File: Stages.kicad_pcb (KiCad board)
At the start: 2 copper layers, 69 x 100 mm, 219 parts, among them IC1 TLC59281, IC10 MCP6002, IC11 LM4040DBZ-2.5, IC12 TL074, IC13 TL074, IC14 TL074, IC2 R-78E3.3-0.5, IC3 4051, IC4 DAC8168, IC5 STM32F373RBTx, IC6 4051, IC7 LD2981ABU33, IC8 MCP6002, IC9 MCP6002, J1 -8.1V to 8.1V, J10 WQP-PJ301M-12_JACK, J11 WQP-PJ301M-12_JACK, J12 WQP-PJ301M-12_JACK, J13 -81V to 8.1V, J14 -81V to 8.1V, J15 -81V to 8.1V, J16 -81V to 8.1V, J17 -81V to 8.1V, J18 -81V to 8.1V, J2 -8.1V to 8.1V, J3 -8.1V to 8.1V, J4 -8.1V to 8.1V, J5 -8.1V to 8.1V, J6 -8.1V to 8.1V, J7 WQP-PJ301M-12_JACK, J8 WQP-PJ301M-12_JACK, J9 WQP-PJ301M-12_JACK, Q1 8MHz, Q2 MMBT3904, Q3 MMBT3904, Q4 MMBT3904, Q5 MMBT3904, Q6 MMBT3904, Q7 MMBT3904, SW1 SW_Push_Dual, SW2 SW_Push_Dual, SW3 SW_Push_Dual, SW4 SW_Push_Dual, SW5 SW_Push_Dual, SW6 SW_Push_Dual

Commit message: Rough Placement Completed
Completed the rough placement of the components on the pcb
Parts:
- D9: footprint Diode_SMD:D_SOT-23_NKA -> Package_TO_SOT_SMD:SOT-23
- IC10, IC8, IC9: footprint Package_SO:MSOP-8-1EP_3x3mm_P0.65mm_EP2.54x2.8mm -> Package_SO:SOIC-8_3.9x4.9mm_P1.27mm
- moved R38 213.0 mm to (140.5, 143.3), turned to 180 degrees
- moved R17 203.8 mm to (165.9, 105.9), turned to 90 degrees
- moved R34 202.6 mm to (116.8, 143.3), turned to 180 degrees
- moved R53 201.4 mm to (137.2, 134.9)
- moved R36 201.2 mm to (125.5, 143.3), turned to 180 degrees
- moved R44 198.5 mm to (137.2, 137.7), turned to 180 degrees
- moved IC6 193.7 mm to (132.3, 89.9), turned to 180 degrees
- moved C22 192.9 mm to (130.8, 96.0), turned to 180 degrees
- moved C47 191.0 mm to (137.2, 140.5), turned to 180 degrees
- moved C53 190.2 mm to (140.5, 146.1), turned to 180 degrees
- moved R57 188.9 mm to (137.2, 132.1), turned to 180 degrees
- moved R62 188.4 mm to (154.7, 135.4), turned to 270 degrees
- moved R40 188.2 mm to (141.0, 97.0), turned to 180 degrees
- moved C35 187.2 mm to (165.1, 115.6)
- moved R35 186.7 mm to (103.4, 143.3), turned to 180 degrees
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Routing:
- net Net-(IC12-Pad10): track 0.00 -> 24.5 mm
- net Net-(IC12-Pad8): track 0.00 -> 16.6 mm
- net Net-(C44-Pad2): track 0.00 -> 12.4 mm
- net Net-(D4-Pad1): track 0.00 -> 12.3 mm
- net Net-(C45-Pad2): track 0.00 -> 11.5 mm
- net Net-(IC12-Pad7): track 0.00 -> 11.2 mm
- net Net-(C44-Pad1): track 0.00 -> 10.4 mm
- net Net-(J5-PadP$1): track 0.00 -> 7.73 mm
- net Net-(IC12-Pad6): track 0.00 -> 6.84 mm
- net Net-(C45-Pad1): track 0.00 -> 6.25 mm
- net Net-(J11-PadP$1): track 0.00 -> 4.18 mm
- net Net-(J6-PadP$1): track 0.00 -> 3.89 mm
- net Net-(J12-PadP$2): track 0.00 -> 2.21 mm
- net Net-(J11-PadP$2): track 0.00 -> 2.19 mm
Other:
- net class Default: clearance 0.2 -> 0.2032; trace_width 0.25 -> 0.381
- net class Power added: clearance 0.2032, trace_width 0.762, via_dia 0.8, via_drill 0.4
- rule trace_clearance: 0.2 -> 0.2032
- rule trace_min: 0.2 -> 0.2032

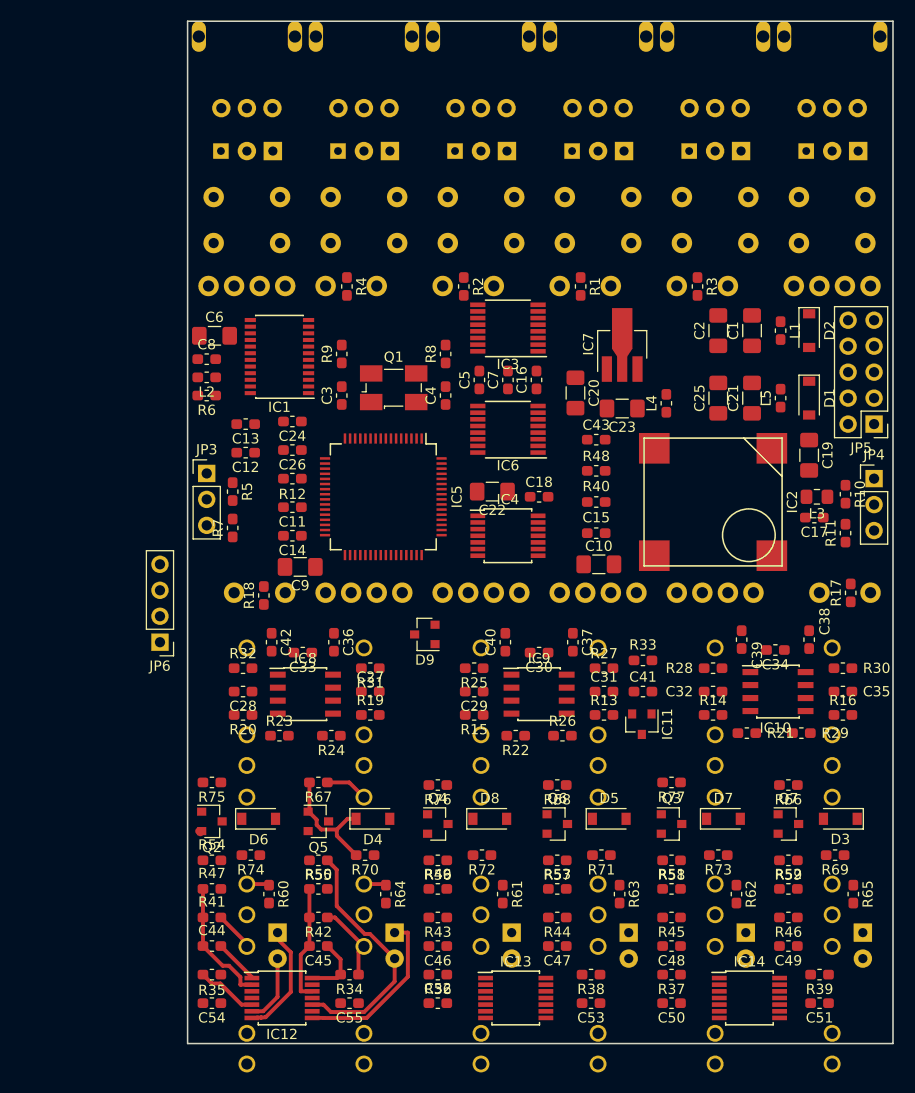
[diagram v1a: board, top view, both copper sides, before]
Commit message: Progress on routing tracks
Most of the power tracks are routed
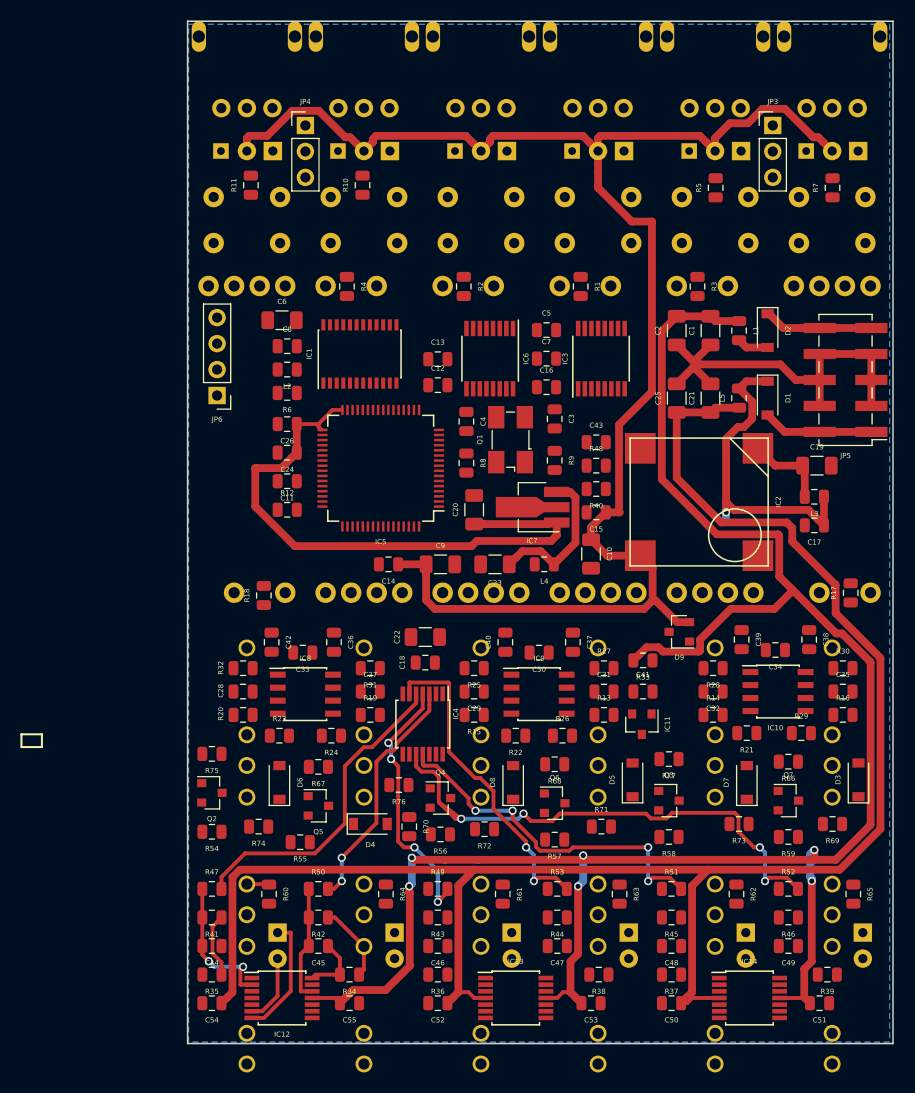
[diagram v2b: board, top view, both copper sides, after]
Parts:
- C1, C10, C19, C2, C20, C21, C22, C23, C25, C6, C9: footprint Capacitor_SMD:C_1206_3216Metric_Pad1.42x1.75mm_HandSolder -> Capacitor_SMD:C_1206_3216Metric
- C11, C12, C13, C14, C15, C16, C17, C18, C24, C26, C27, C28, C29, C3, C30, C31, C32, C33, C34, C35, C36, C37, C38, C39, C4, C40, C41, C42, C43, C44, C45, C46, C47, C48, C49, C5, C50, C51, C52, C53, C54, C55, C7, C8: footprint Capacitor_SMD:C_0603_1608Metric_Pad1.05x0.95mm_HandSolder -> Capacitor_SMD:C_0805_2012Metric
- JP5: footprint Connector_PinHeader_2.54mm:PinHeader_2x05_P2.54mm_Vertical -> Connector_PinHeader_2.54mm:PinHeader_2x05_P2.54mm_Vertical_SMD
- L1, L2, L4, L5, R1, R10, R11, R12, R13, R14, R15, R16, R17, R18, R19, R2, R20, R21, R22, R23, R24, R25, R26, R27, R28, R29, R3, R30, R31, R32, R33, R34, R35, R36, R37, R38, R39, R4, R40, R41, R42, R43, R44, R45, R46, R47, R48, R49, R5, R50, R51, R52, R53, R54, R55, R56, R57, R58, R59, R6, R60, R61, R62, R63, R64, R65, R66, R67, R68, R69, R7, R70, R71, R72, R73, R74, R75, R76, R77, R8, R9: footprint Resistor_SMD:R_0603_1608Metric_Pad1.05x0.95mm_HandSolder -> Resistor_SMD:R_0805_2012Metric
- L3: footprint Inductor_SMD:L_0805_2012Metric_Pad1.15x1.40mm_HandSolder -> Inductor_SMD:L_0805_2012Metric
- moved R7 67.5 mm to (164.1, 66.3)
- moved R11 67.4 mm to (107.2, 66.0)
- moved JP4 65.5 mm to (112.5, 60.2)
- moved JP3 65.0 mm to (158.2, 60.2)
- moved R10 56.1 mm to (118.1, 66.0), turned to 90 degrees
- moved R5 55.8 mm to (152.7, 66.3), turned to 90 degrees
- moved D9 24.9 mm to (149.1, 109.7)
- moved JP6 24.8 mm to (103.9, 86.6)
- moved R9 23.3 mm to (136.9, 93.0), turned to 270 degrees
- moved C3 21.0 mm to (136.9, 88.9), turned to 270 degrees
- moved IC4 20.2 mm to (124.0, 118.8), turned to 270 degrees
- moved C12 19.9 mm to (125.5, 85.6), turned to 0 degrees
- moved C13 19.8 mm to (125.5, 83.1), turned to 0 degrees
- moved L4 19.8 mm to (135.9, 103.1), turned to 180 degrees
- moved C23 19.7 mm to (131.1, 103.1)
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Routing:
- net VEE: track 0.00 -> 195.1 mm, vias 0 -> 6
- net VCC: track 0.00 -> 172.3 mm
- net +3V3: track 0.00 -> 158.8 mm
- net +3V3_A: track 0.00 -> 57.8 mm
- net DAC_1: track 0.00 -> 51.9 mm, vias 0 -> 4
- net 4051GND: track 0.18 -> 38.3 mm
- net DAC_2: track 0.00 -> 34.9 mm, vias 0 -> 4
- net DAC_3: track 0.00 -> 31.9 mm, vias 0 -> 2
- net DAC_6: track 0.00 -> 31.4 mm
- net Net-(C17-Pad1): track 0.00 -> 31.0 mm, vias 0 -> 1
- net DAC_4: track 0.00 -> 26.0 mm, vias 0 -> 4
- net Net-(IC12-Pad10): track 24.5 -> 0.00 mm
- net DAC_5: track 0.00 -> 23.9 mm, vias 0 -> 2
- net Net-(IC12-Pad8): track 16.6 -> 0.00 mm
- net Net-(C23-Pad1): track 0.00 -> 14.9 mm
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- added copper zone on B.Cu, net 4051GND
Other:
- net class Default: via_drill 0.4 -> 0.5
- net class Power: via_drill 0.4 -> 0.5

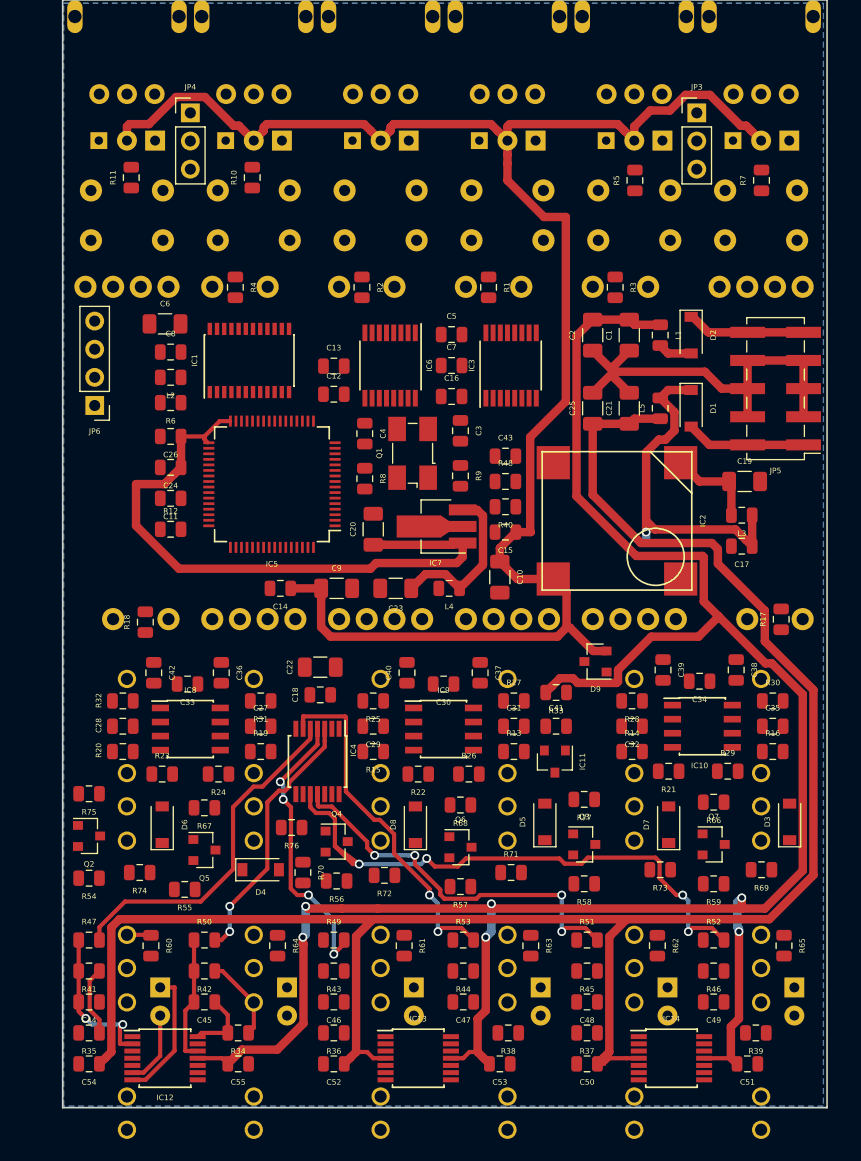
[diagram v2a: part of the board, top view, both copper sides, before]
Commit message: Re-oriented several components
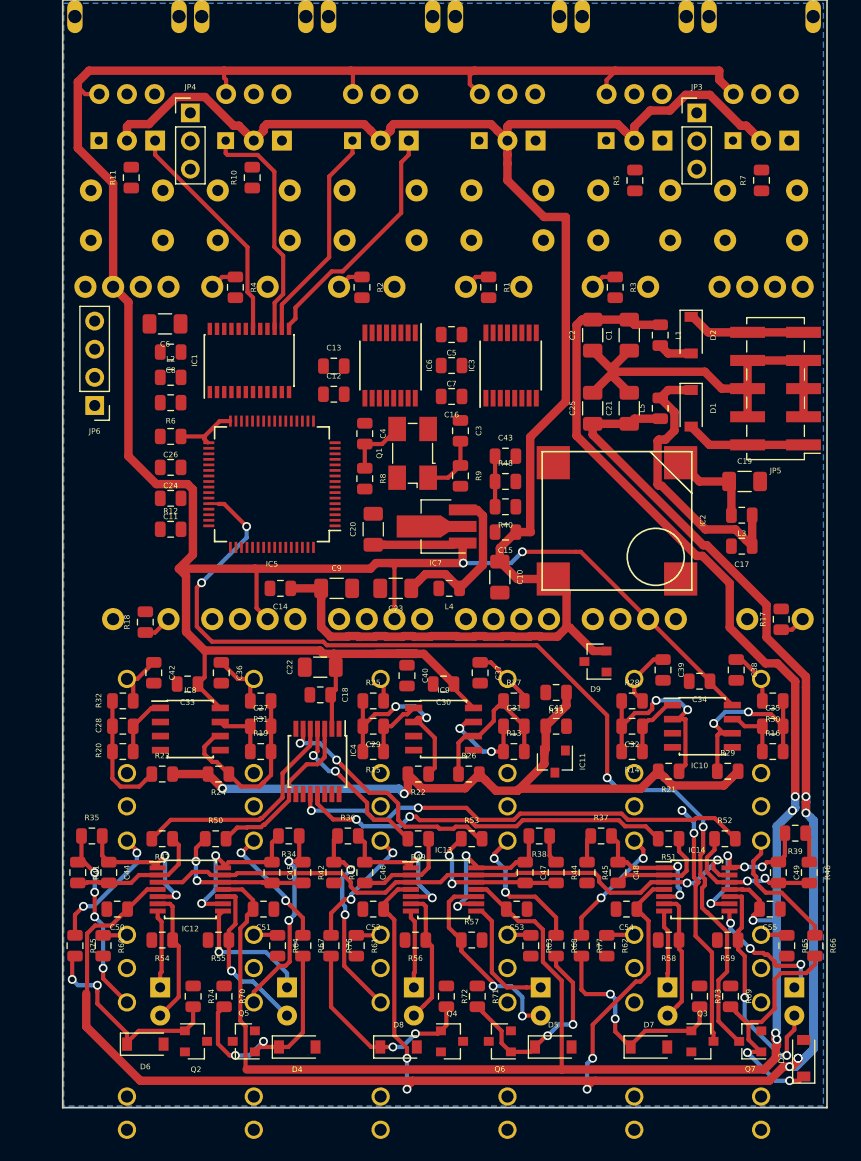
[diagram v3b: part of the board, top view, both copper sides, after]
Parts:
- moved C54 50.5 mm to (151.9, 132.1)
- moved C55 50.0 mm to (164.8, 132.1)
- moved C51 45.9 mm to (119.1, 132.1)
- moved C50 44.7 mm to (105.9, 132.1)
- moved D3 21.4 mm to (167.9, 145.5)
- moved Q2 20.9 mm to (113.0, 144.0)
- moved Q4 20.8 mm to (136.1, 144.0)
- moved Q3 20.7 mm to (158.8, 144.0)
- moved D5 20.3 mm to (145.3, 144.5), turned to 0 degrees
- moved D7 20.1 mm to (153.9, 144.5), turned to 0 degrees
- moved D8 20.1 mm to (131.3, 144.5), turned to 0 degrees
- moved D6 19.9 mm to (108.5, 144.3), turned to 0 degrees
- moved R39 18.4 mm to (167.1, 125.2)
- moved R34 18.4 mm to (121.4, 125.5)
- moved Q7 18.1 mm to (163.1, 144.0), turned to 180 degrees
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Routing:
- net +3V3_A: track 57.8 -> 259.1 mm, vias 0 -> 2
- net GATE_1: track 0.00 -> 94.2 mm, vias 0 -> 4
- net AREF_-2.5: track 0.00 -> 67.6 mm, vias 0 -> 2
- net VREF_BIAS: track 0.00 -> 62.3 mm, vias 0 -> 2
- net VCC: track 172.3 -> 224.4 mm, vias 0 -> 9
- net Net-(D3-Pad1): track 0.00 -> 23.4 mm, vias 0 -> 2
- net GATE_2: track 0.00 -> 22.2 mm, vias 0 -> 2
- net Net-(IC1-Pad13): track 0.00 -> 22.1 mm
- net Net-(D4-Pad1): track 0.00 -> 21.9 mm, vias 0 -> 2
- net Net-(IC14-Pad10): track 0.00 -> 21.6 mm, vias 0 -> 2
- net Net-(IC1-Pad15): track 0.00 -> 21.1 mm
- net Net-(IC1-Pad18): track 0.00 -> 20.7 mm
- net Net-(D7-Pad1): track 0.00 -> 20.0 mm, vias 0 -> 2
- net Net-(C32-Pad2): track 0.00 -> 19.9 mm, vias 0 -> 2
- net Net-(IC1-Pad14): track 0.00 -> 19.6 mm
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
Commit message: Re-orientation
Fixed some bad op-amp orientations
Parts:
- moved C20 38.8 mm to (167.4, 103.4), turned to 0 degrees
- moved C43 37.2 mm to (104.6, 99.1), turned to 90 degrees
- moved C23 37.0 mm to (167.3, 95.4)
- moved R48 34.5 mm to (106.9, 99.1), turned to 90 degrees
- moved IC3 34.1 mm to (107.4, 82.0), turned to 0 degrees
- moved L4 33.5 mm to (167.8, 92.9)
- moved C5 32.3 mm to (104.6, 87.4), turned to 270 degrees
- moved IC7 31.0 mm to (166.0, 99.5)
- moved C7 29.1 mm to (107.4, 87.4), turned to 270 degrees
- moved JP6 28.6 mm to (131.1, 95.5)
- moved C16 26.0 mm to (110.2, 87.4), turned to 270 degrees
- moved C6 25.9 mm to (136.1, 80.3)
- moved C8 25.9 mm to (136.7, 82.8)
- moved L2 25.9 mm to (136.7, 85.1)
- moved R6 25.9 mm to (136.7, 87.4)
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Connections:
- IC12 pad 10: Net-(IC12-Pad10) -> Net-(C45-Pad1)
- IC12 pad 12: Net-(C45-Pad2) -> VREF_BIAS
- IC12 pad 13: VREF_BIAS -> Net-(C45-Pad2)
- IC12 pad 9: Net-(C45-Pad1) -> Net-(IC12-Pad9)
- IC13 pad 10: Net-(IC13-Pad10) -> Net-(C47-Pad1)
- IC13 pad 12: Net-(C47-Pad2) -> VREF_BIAS
- IC13 pad 13: VREF_BIAS -> Net-(C47-Pad2)
- IC13 pad 9: Net-(C47-Pad1) -> Net-(IC13-Pad9)
- IC14 pad 10: Net-(IC14-Pad10) -> Net-(C49-Pad1)
- IC14 pad 12: Net-(C49-Pad2) -> VREF_BIAS
- IC14 pad 13: VREF_BIAS -> Net-(C49-Pad2)
- IC14 pad 9: Net-(C49-Pad1) -> Net-(IC14-Pad9)
- LED1 pad 2: Net-(IC14-Pad10) -> Net-(IC14-Pad9)
- LED2 pad 2: Net-(IC13-Pad10) -> Net-(IC13-Pad9)
- LED6 pad 2: Net-(IC12-Pad10) -> Net-(IC12-Pad9)
- R55 pad 1: Net-(IC12-Pad10) -> Net-(IC12-Pad9)
- R57 pad 1: Net-(IC13-Pad10) -> Net-(IC13-Pad9)
- R59 pad 1: Net-(IC14-Pad10) -> Net-(IC14-Pad9)
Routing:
- net +3V3: track 159.1 -> 61.9 mm, vias 0 -> 2
- net GATE_1: track 94.2 -> 0.00 mm, vias 4 -> 0
- net VCC: track 224.4 -> 133.8 mm, vias 9 -> 8
- net VREF_BIAS: track 62.3 -> 0.00 mm, vias 2 -> 0
- net AREF_-2.5: track 67.6 -> 8.12 mm, vias 2 -> 0
- net DAC_1: track 42.3 -> 0.00 mm, vias 2 -> 0
- net 4051GND: track 38.3 -> 0.00 mm
- net +3V3_A: track 259.1 -> 297.1 mm, vias 2 -> 0
- net DAC_2: track 34.1 -> 0.00 mm, vias 2 -> 0
- net LEDS_SIN: track 0.00 -> 23.5 mm
- net Net-(D3-Pad1): track 23.4 -> 0.00 mm, vias 2 -> 0
- net POTS_ADDR_B: track 0.00 -> 23.3 mm, vias 0 -> 2
- net LEDS_SS: track 0.00 -> 23.0 mm
- net LEDS_SCK: track 0.00 -> 23.0 mm
- net POTS_ADDR_A: track 0.00 -> 22.7 mm, vias 0 -> 2
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
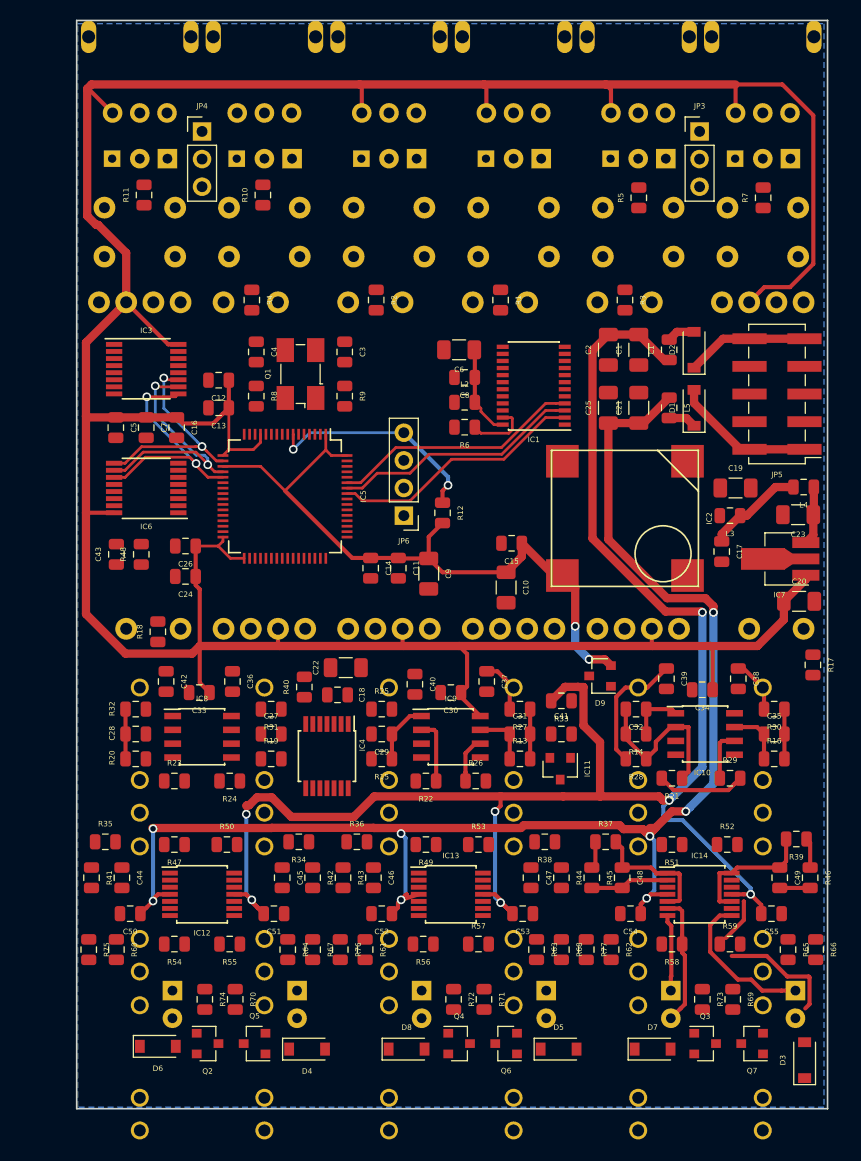
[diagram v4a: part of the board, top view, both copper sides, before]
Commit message: Added Mounting Holes
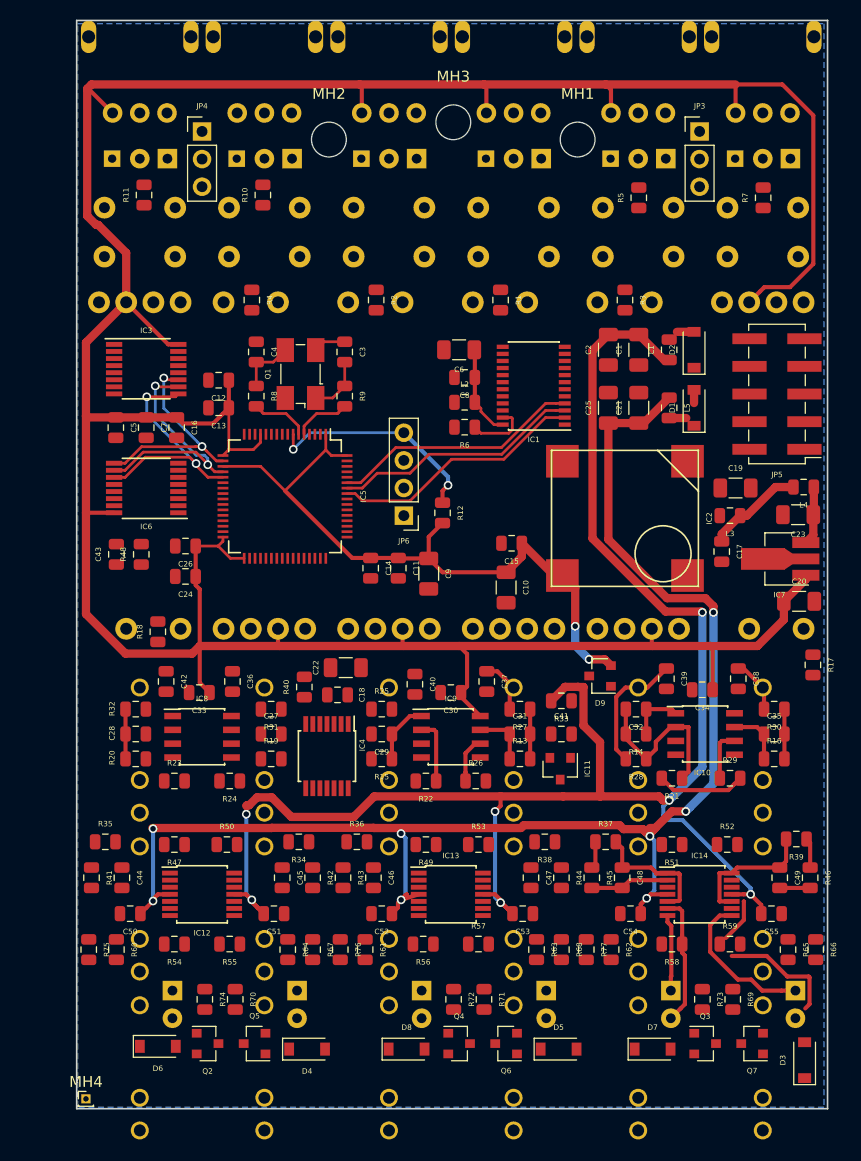
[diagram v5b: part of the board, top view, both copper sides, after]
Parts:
- added MH1: MountingHole, MountingHole:MountingHole_3.2mm_M3, F.Cu at (147.0, 60.9)
- added MH2: MountingHole, MountingHole:MountingHole_3.2mm_M3, F.Cu at (124.2, 60.9)
- added MH3: MountingHole, MountingHole:MountingHole_3.2mm_M3, F.Cu at (135.6, 59.4)
- added MH4: MountingHole_Pad, Connector_PinHeader_1.00mm:PinHeader_1x01_P1.00mm_Vertical, F.Cu at (101.9, 149.1)
- J13, J14, J15, J16, J17, J18: value -81V to 8.1V -> -8.1V to 8.1V
- SW1, SW2, SW3, SW4, SW5, SW6: value SW_Push_Dual -> SW_Push_4pin
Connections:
- D1 pad 1: Net-(C17-Pad1) -> Net-(D1-Pad1)
- D2 pad 1: Net-(D2-Pad1) -> Net-(C17-Pad1)
- JP5 pad 1: Net-(D1-Pad2) -> Net-(D2-Pad2)
- JP5 pad 10: Net-(D2-Pad1) -> Net-(D1-Pad1)
- JP5 pad 2: Net-(D1-Pad2) -> Net-(D2-Pad2)
- JP5 pad 9: Net-(D2-Pad1) -> Net-(D1-Pad1)
- L1 pad 2: Net-(D2-Pad2) -> Net-(D1-Pad2)
- R5 pad 1: LEFT_RX -> LEFT_TX
- R7 pad 1: LEFT_TX -> LEFT_RX
- SW1 pad 2: SW_MODE_1 -> 4051GND
- SW1 pad 3: 4051GND -> SW_MODE_1
- SW2 pad 2: SW_MODE_2 -> 4051GND
- SW2 pad 3: 4051GND -> SW_MODE_2
- SW3 pad 2: SW_MODE_3 -> 4051GND
- SW3 pad 3: 4051GND -> SW_MODE_3
- SW4 pad 2: SW_MODE_4 -> 4051GND
- SW4 pad 3: 4051GND -> SW_MODE_4
- SW5 pad 2: SW_MODE_5 -> 4051GND
- SW5 pad 3: 4051GND -> SW_MODE_5
- SW6 pad 2: SW_MODE_6 -> 4051GND
- SW6 pad 3: 4051GND -> SW_MODE_6
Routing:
- net Net-(D1-Pad2): track 13.1 -> 1.21 mm
- net Net-(D2-Pad1): track 11.2 -> 0.00 mm
- net Net-(IC5-Pad6): track 0.00 -> 5.39 mm
- net Net-(C4-Pad2): track 0.00 -> 5.31 mm
- net Net-(C3-Pad2): track 0.00 -> 5.31 mm
- net Net-(IC5-Pad5): track 0.00 -> 5.24 mm
- net 4051GND: track 0.00 -> 2.98 mm
- net Net-(C17-Pad1): track 11.6 -> 10.6 mm
- net Net-(D2-Pad2): track 2.58 -> 1.57 mm
